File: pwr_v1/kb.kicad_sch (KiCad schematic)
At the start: 12 parts, among them J1 Conn_01x12_Pin, Q1 BSS84

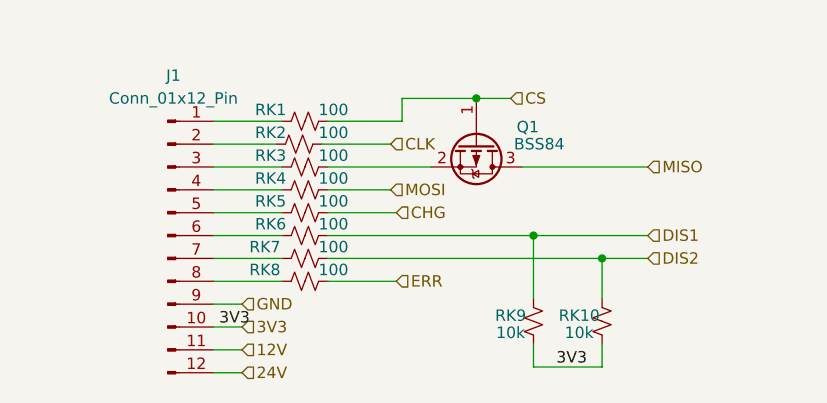
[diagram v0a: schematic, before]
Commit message: Schematic and layout updated; Layout placement and routing completed
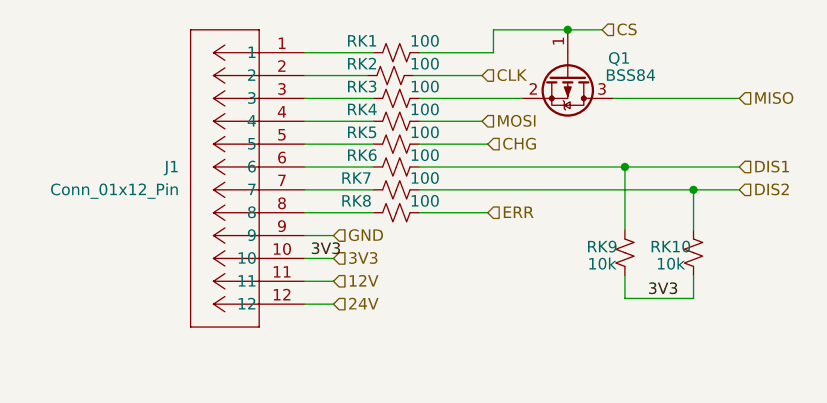
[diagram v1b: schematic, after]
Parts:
- J1: footprint (none) -> 12pConn:CON12_1X12_UR_DF13; symbol Connector:Conn_01x12_Pin -> Hirose_12PConn:DF13-12P-1.25DS20
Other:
- moved on the sheet: Q1, RK1, RK10, RK2, RK3, RK4, RK5, RK6, RK7, RK8, RK9

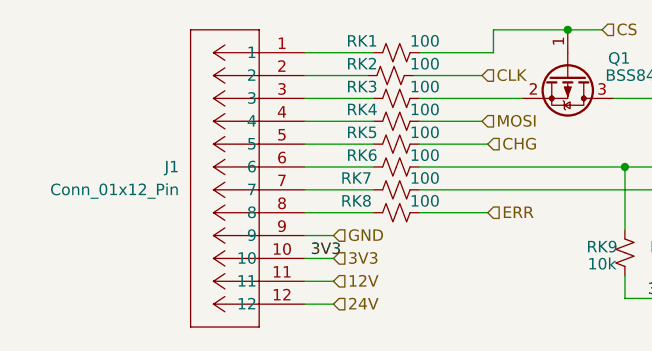
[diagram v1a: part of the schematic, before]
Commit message: Sch: DNP updated, JLC part numbers updated for all components; Lay: Fiducial placement, routing aligned.
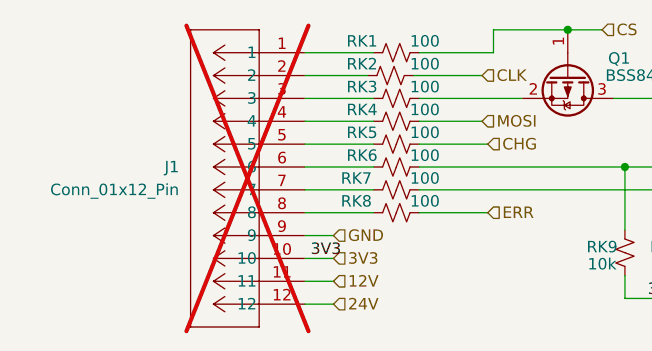
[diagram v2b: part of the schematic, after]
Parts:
- J1: now not fitted; now left out of the parts list
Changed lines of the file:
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@@
 		(unit 1)
 		(exclude_from_sim no)
-		(in_bom yes)
+		(in_bom no)
 		(on_board yes)
-		(dnp no)
+		(dnp yes)
 		(property "Reference" "J1"
 			(at 73.66 60.9599 0)

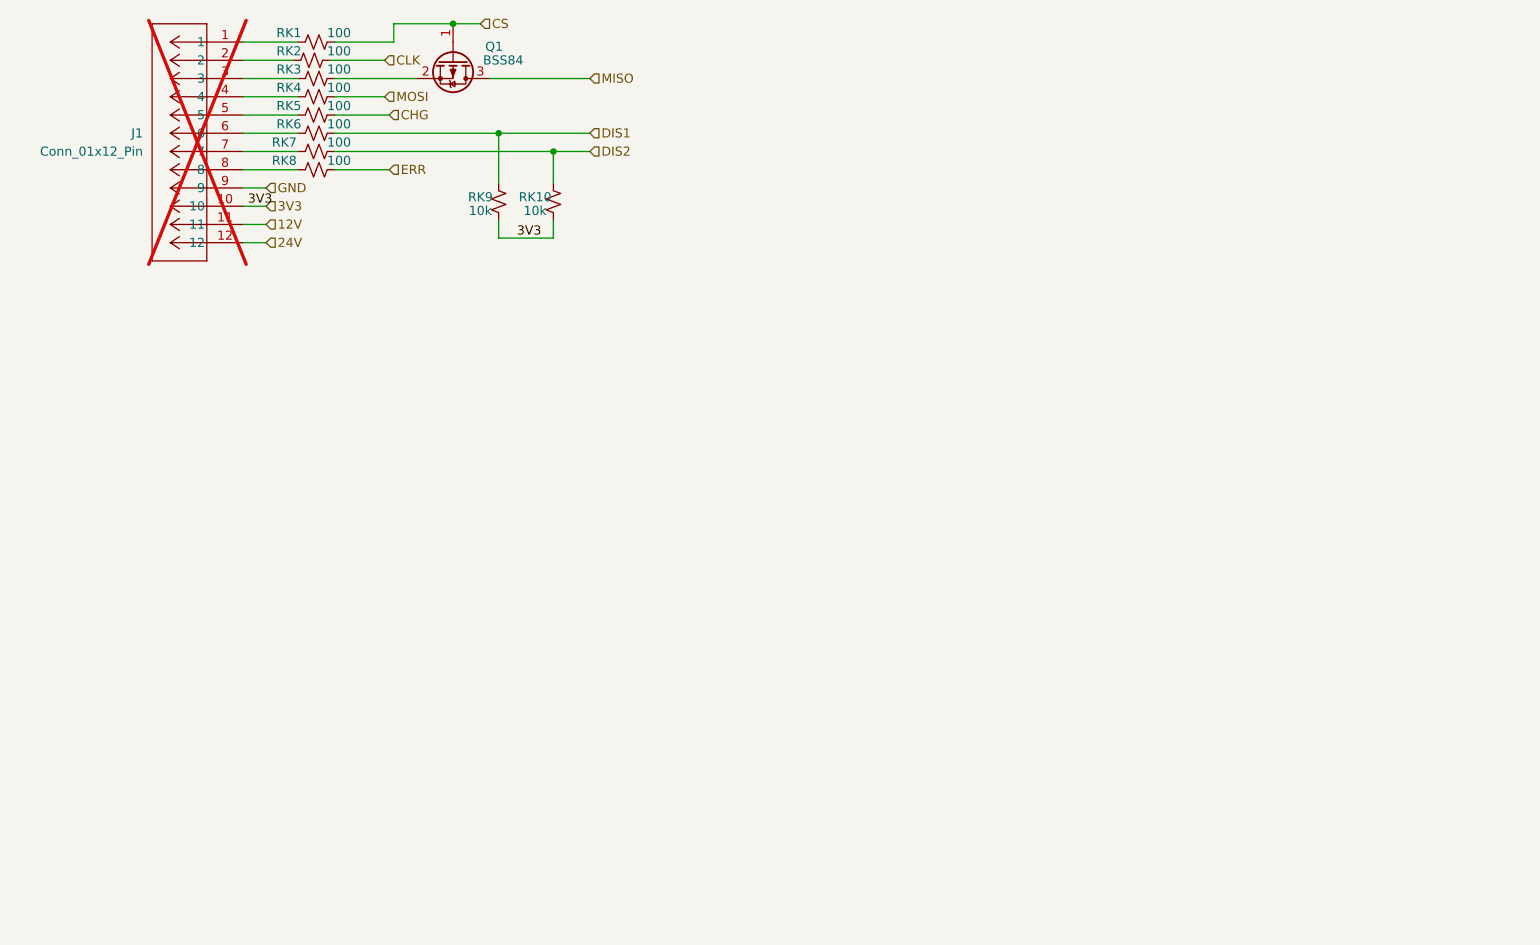
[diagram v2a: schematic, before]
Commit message: File structure enhanced.
Added uniform titleblocks and 3D renders for easier view, file cleanups.
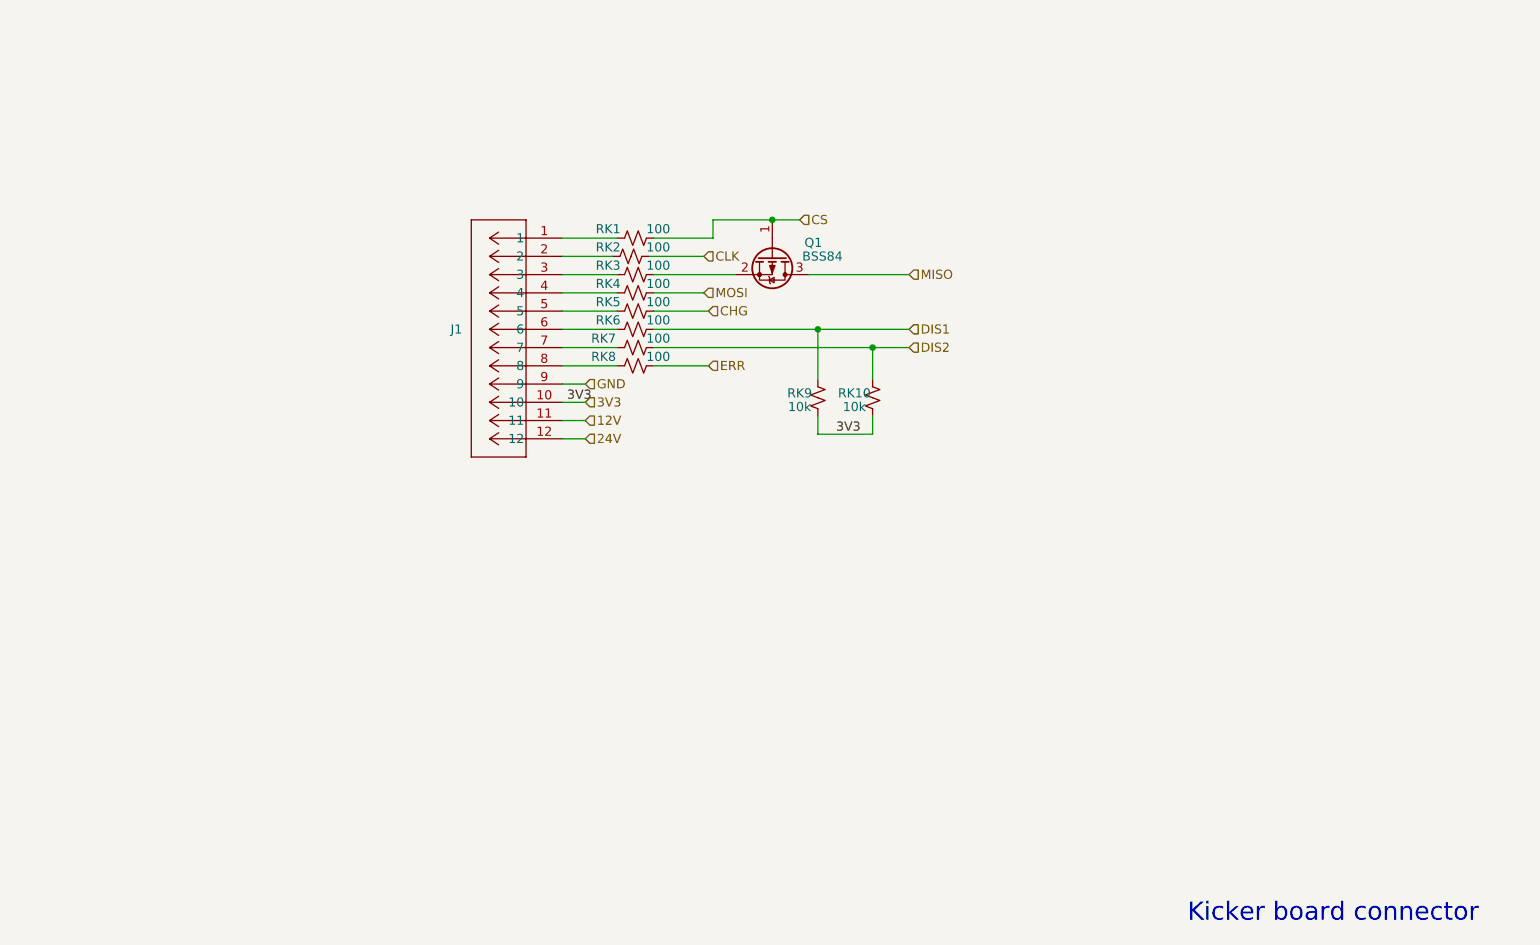
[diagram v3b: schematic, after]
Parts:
- J1: now fitted
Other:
- note added: "Kicker board connector"
- title: (none) -> Power board
- moved on the sheet: Q1, RK1, RK10, RK2, RK3, RK4, RK5, RK6, RK7, RK8, RK9
